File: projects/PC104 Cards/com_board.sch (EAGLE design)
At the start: 7 parts, among them J2 M22-6013005, U2 ESP32-DEVKITC-32D

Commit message: Updated PCB Designs
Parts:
- removed SV1: (no value), con-lsta:FE08-1
- added SV2: (no value), con-lsta:FE12-1
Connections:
- net D18: now also SV2.4; no longer SV1.3
- net D19: now also SV2.3; no longer SV1.2
- net D2: now also SV2.2; no longer SV1.1
- net D21: now also SV2.6; no longer SV1.5
- net D22: now also SV2.7; no longer SV1.6
- net D23: now also SV2.12; no longer SV1.8
- net D4: now also SV2.5; no longer SV1.4
- net GND1: now also SV2.11; no longer SV1.7
- net GND2: now also SV2.10
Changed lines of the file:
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@@
 <part name="H3" library="holes" library_urn="urn:adsk.eagle:library:237" deviceset="MOUNT-PAD-ROUND" device="3.2" package3d_urn="urn:adsk.eagle:package:14282/1"/>
 <part name="H4" library="holes" library_urn="urn:adsk.eagle:library:237" deviceset="MOUNT-PAD-ROUND" device="3.2" package3d_urn="urn:adsk.eagle:package:14282/1"/>
-<part name="SV1" library="con-lsta" library_urn="urn:adsk.eagle:library:161" deviceset="FE08-1" device="" package3d_urn="urn:adsk.eagle:package:8194/1"/>
 <part name="U2" library="ESP32-DEVKITC-32D" deviceset="ESP32-DEVKITC-32D" device=""/>
 <part name="J2" library="M22-6013005" deviceset="M22-6013005" device=""/>
+<part name="SV2" library="con-lsta" library_urn="urn:adsk.eagle:library:161" deviceset="FE12-1" device="" package3d_urn="urn:adsk.eagle:package:8193/1"/>
 </parts>
 <sheets>
@@
 <attribute name="VALUE" x="283.464" y="-102.7938" size="1.778" layer="96"/>
 </instance>
-<instance part="SV1" gate="G$1" x="414.02" y="-76.2" smashed="yes">
-<attribute name="VALUE" x="412.75" y="-88.9" size="1.778" layer="96"/>
-<attribute name="NAME" x="412.75" y="-62.738" size="1.778" layer="95"/>
-</instance>
 <instance part="U2" gate="G$1" x="353.06" y="68.58" smashed="yes">
 <attribute name="NAME" x="337.8028" y="94.6443" size="1.78" layer="95"/>
@@
 <attribute name="NAME" x="502.92" y="13.208" size="1.778" layer="95" rot="R180"/>
 <attribute name="VALUE" x="502.92" y="168.91" size="1.778" layer="96" rot="R180"/>
+</instance>
+<instance part="SV2" gate="G$1" x="368.3" y="-78.74" smashed="yes">
+<attribute name="VALUE" x="367.03" y="-96.52" size="1.778" layer="96"/>
+<attribute name="NAME" x="367.03" y="-60.198" size="1.778" layer="95"/>
 </instance>
 </instances>
@@
 <net name="GND1" class="0">
 <segment>
-<wire x1="421.64" y1="-68.58" x2="431.8" y2="-68.58" width="0.1524" layer="91"/>
-<label x="431.8" y="-68.58" size="1.778" layer="95" xref="yes"/>
-<pinref part="SV1" gate="G$1" pin="7"/>
+<pinref part="SV2" gate="G$1" pin="11"/>
+<wire x1="375.92" y1="-66.04" x2="388.62" y2="-66.04" width="0.1524" layer="91"/>
+<label x="388.62" y="-66.04" size="1.778" layer="95" xref="yes"/>
 </segment>
 </net>
@@
 <label x="513.08" y="46.99" size="1.778" layer="95" xref="yes"/>
 </segment>
+<segment>
+<pinref part="SV2" gate="G$1" pin="10"/>
+<wire x1="375.92" y1="-68.58" x2="381" y2="-68.58" width="0.1524" layer="91"/>
+<label x="381" y="-68.58" size="1.778" layer="95" xref="yes"/>
+</segment>
 </net>
 <net name="GND4" class="0">
@@
 <net name="D23" class="0">
 <segment>
-<wire x1="421.64" y1="-66.04" x2="441.96" y2="-66.04" width="0.1524" layer="91"/>
-<label x="441.96" y="-66.04" size="1.778" layer="95" xref="yes"/>
-<pinref part="SV1" gate="G$1" pin="8"/>
-</segment>
-<segment>
 <pinref part="U2" gate="G$1" pin="IO0"/>
 <wire x1="373.38" y1="58.42" x2="381" y2="58.42" width="0.1524" layer="91"/>
 <label x="381" y="58.42" size="1.27" layer="95" xref="yes"/>
 </segment>
+<segment>
+<pinref part="SV2" gate="G$1" pin="12"/>
+<wire x1="375.92" y1="-63.5" x2="381" y2="-63.5" width="0.1524" layer="91"/>
+<label x="381" y="-63.5" size="1.778" layer="95" xref="yes"/>
+</segment>
 </net>
 <net name="D22" class="0">
-<segment>
-<wire x1="421.64" y1="-71.12" x2="424.18" y2="-71.12" width="0.1524" layer="91"/>
-<label x="424.18" y="-71.12" size="1.778" layer="95" xref="yes"/>
-<pinref part="SV1" gate="G$1" pin="6"/>
-</segment>
 <segment>
 <pinref part="U2" gate="G$1" pin="IO2"/>
@@
 <label x="381" y="55.88" size="1.27" layer="95" xref="yes"/>
 </segment>
+<segment>
+<pinref part="SV2" gate="G$1" pin="7"/>
+<wire x1="375.92" y1="-76.2" x2="388.62" y2="-76.2" width="0.1524" layer="91"/>
+<label x="388.62" y="-76.2" size="1.778" layer="95" xref="yes"/>
+</segment>
 </net>
 <net name="D21" class="0">
-<segment>
-<wire x1="421.64" y1="-73.66" x2="441.96" y2="-73.66" width="0.1524" layer="91"/>
-<label x="441.96" y="-73.66" size="1.778" layer="95" xref="yes"/>
-<pinref part="SV1" gate="G$1" pin="5"/>
-</segment>
 <segment>
 <pinref part="U2" gate="G$1" pin="IO15"/>
@@
 <label x="381" y="53.34" size="1.27" layer="95" xref="yes"/>
 </segment>
+<segment>
+<pinref part="SV2" gate="G$1" pin="6"/>
+<wire x1="375.92" y1="-78.74" x2="381" y2="-78.74" width="0.1524" layer="91"/>
+<label x="381" y="-78.74" size="1.778" layer="95" xref="yes"/>
+</segment>
 </net>
 <net name="D19" class="0">
-<segment>
-<wire x1="421.64" y1="-81.28" x2="441.96" y2="-81.28" width="0.1524" layer="91"/>
-<label x="441.96" y="-81.28" size="1.778" layer="95" xref="yes"/>
-<pinref part="SV1" gate="G$1" pin="2"/>
-</segment>
 <segment>
 <pinref part="U2" gate="G$1" pin="IO14"/>
@@
 <label x="294.64" y="63.5" size="1.27" layer="95" rot="R180" xref="yes"/>
 </segment>
+<segment>
+<pinref part="SV2" gate="G$1" pin="3"/>
+<wire x1="375.92" y1="-86.36" x2="388.62" y2="-86.36" width="0.1524" layer="91"/>
+<label x="388.62" y="-86.36" size="1.778" layer="95" xref="yes"/>
+</segment>
 </net>
 <net name="D18" class="0">
-<segment>
-<wire x1="421.64" y1="-78.74" x2="424.18" y2="-78.74" width="0.1524" layer="91"/>
-<label x="424.18" y="-78.74" size="1.778" layer="95" xref="yes"/>
-<pinref part="SV1" gate="G$1" pin="3"/>
-</segment>
 <segment>
 <pinref part="U2" gate="G$1" pin="IO13"/>
@@
 <label x="312.42" y="55.88" size="1.27" layer="95" rot="R180" xref="yes"/>
 </segment>
+<segment>
+<pinref part="SV2" gate="G$1" pin="4"/>
+<wire x1="375.92" y1="-83.82" x2="381" y2="-83.82" width="0.1524" layer="91"/>
+<label x="381" y="-83.82" size="1.778" layer="95" xref="yes"/>
+</segment>
 </net>
 <net name="D4" class="0">
-<segment>
-<wire x1="421.64" y1="-76.2" x2="434.34" y2="-76.2" width="0.1524" layer="91"/>
-<label x="434.34" y="-76.2" size="1.778" layer="95" xref="yes"/>
-<pinref part="SV1" gate="G$1" pin="4"/>
-</segment>
 <segment>
 <pinref part="U2" gate="G$1" pin="IO27"/>
@@
 <label x="294.64" y="66.04" size="1.27" layer="95" rot="R180" xref="yes"/>
 </segment>
+<segment>
+<pinref part="SV2" gate="G$1" pin="5"/>
+<wire x1="375.92" y1="-81.28" x2="388.62" y2="-81.28" width="0.1524" layer="91"/>
+<label x="388.62" y="-81.28" size="1.778" layer="95" xref="yes"/>
+</segment>
 </net>
 <net name="D2" class="0">
-<segment>
-<wire x1="421.64" y1="-83.82" x2="431.8" y2="-83.82" width="0.1524" layer="91"/>
-<label x="431.8" y="-83.82" size="1.778" layer="95" xref="yes"/>
-<pinref part="SV1" gate="G$1" pin="1"/>
-</segment>
 <segment>
 <pinref part="U2" gate="G$1" pin="IO5"/>
@@
 <label x="375.92" y="68.58" size="1.27" layer="95" xref="yes"/>
 </segment>
-</net>
+<segment>
+<pinref part="SV2" gate="G$1" pin="2"/>
+<wire x1="375.92" y1="-88.9" x2="381" y2="-88.9" width="0.1524" layer="91"/>
+<label x="381" y="-88.9" size="1.778" layer="95" xref="yes"/>
+</segment>
+</net>

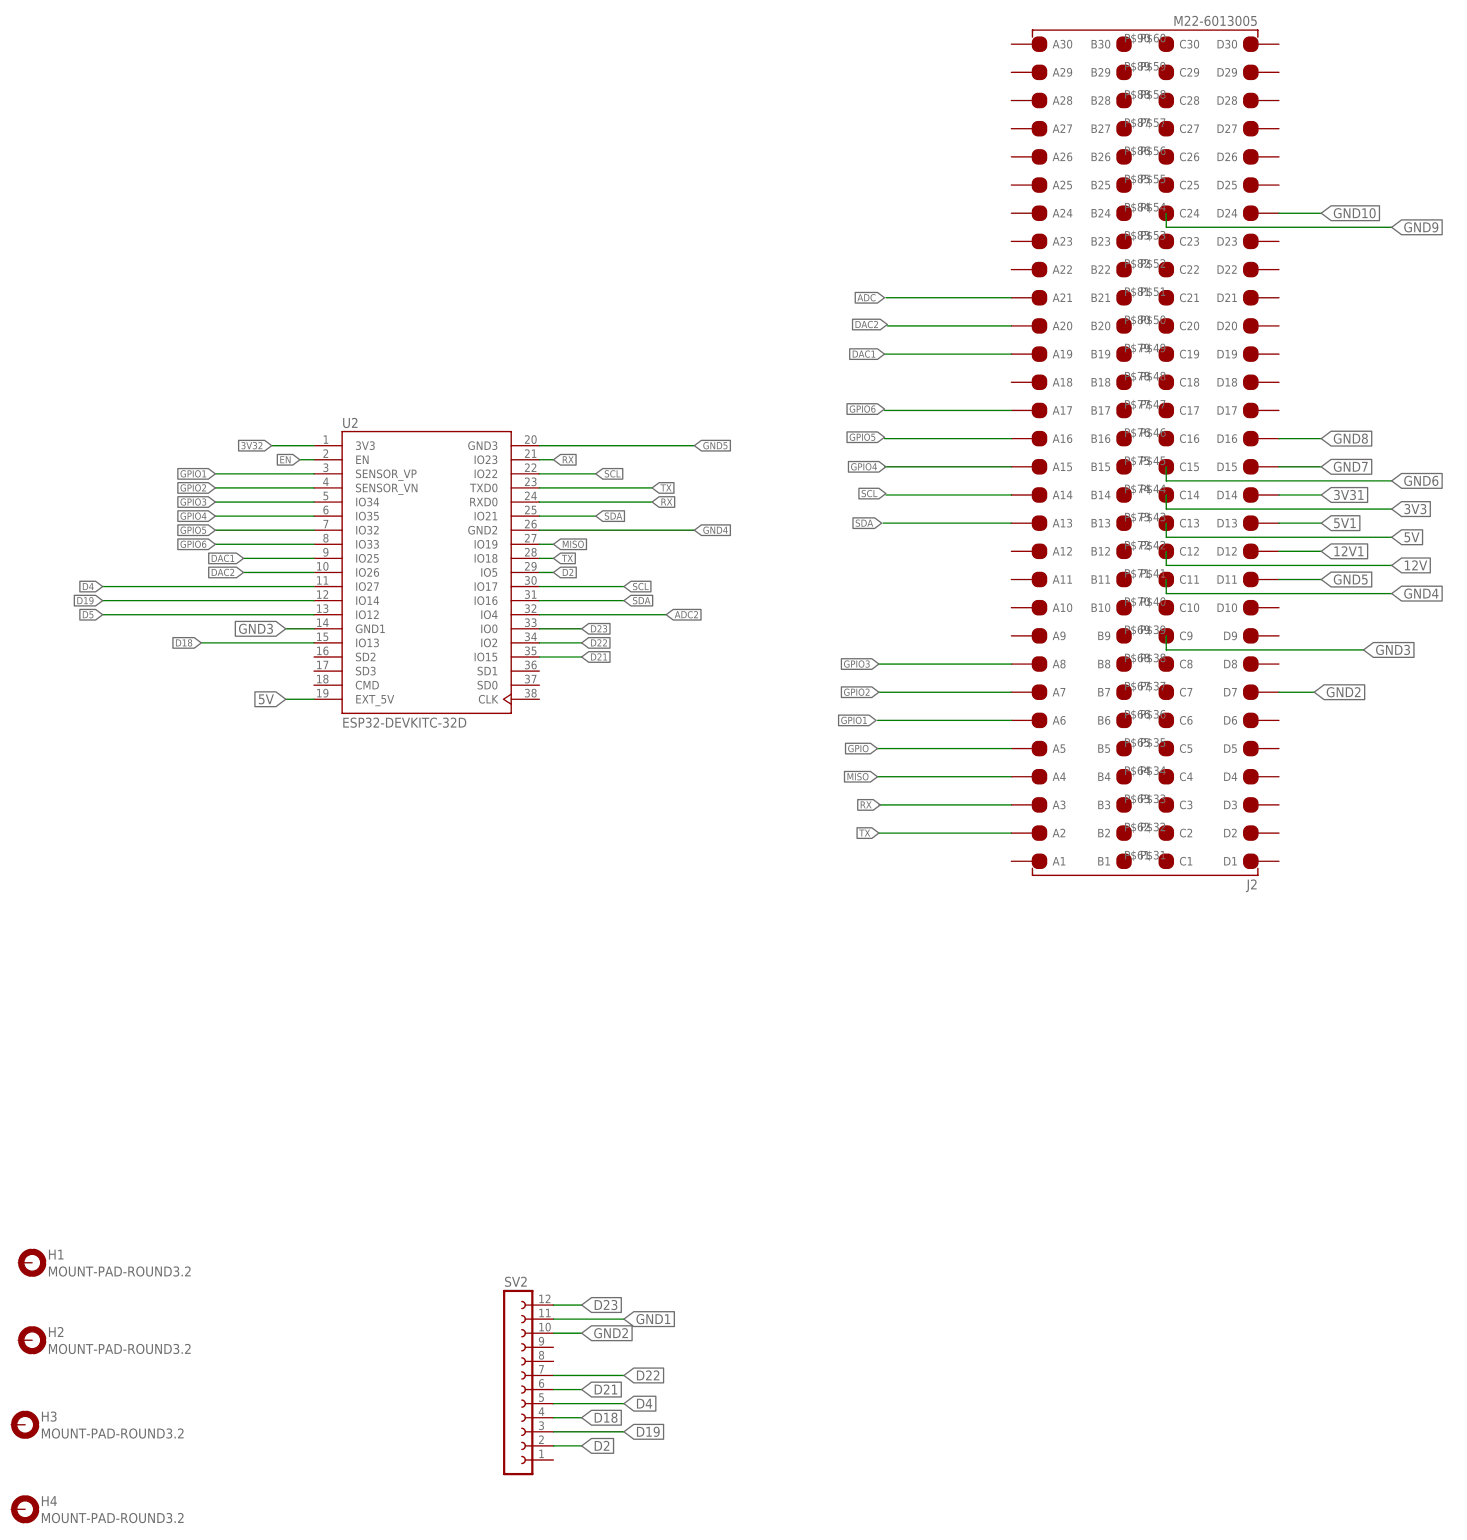
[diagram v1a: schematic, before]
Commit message: Updated PCB desgins to fix wiring mismatches
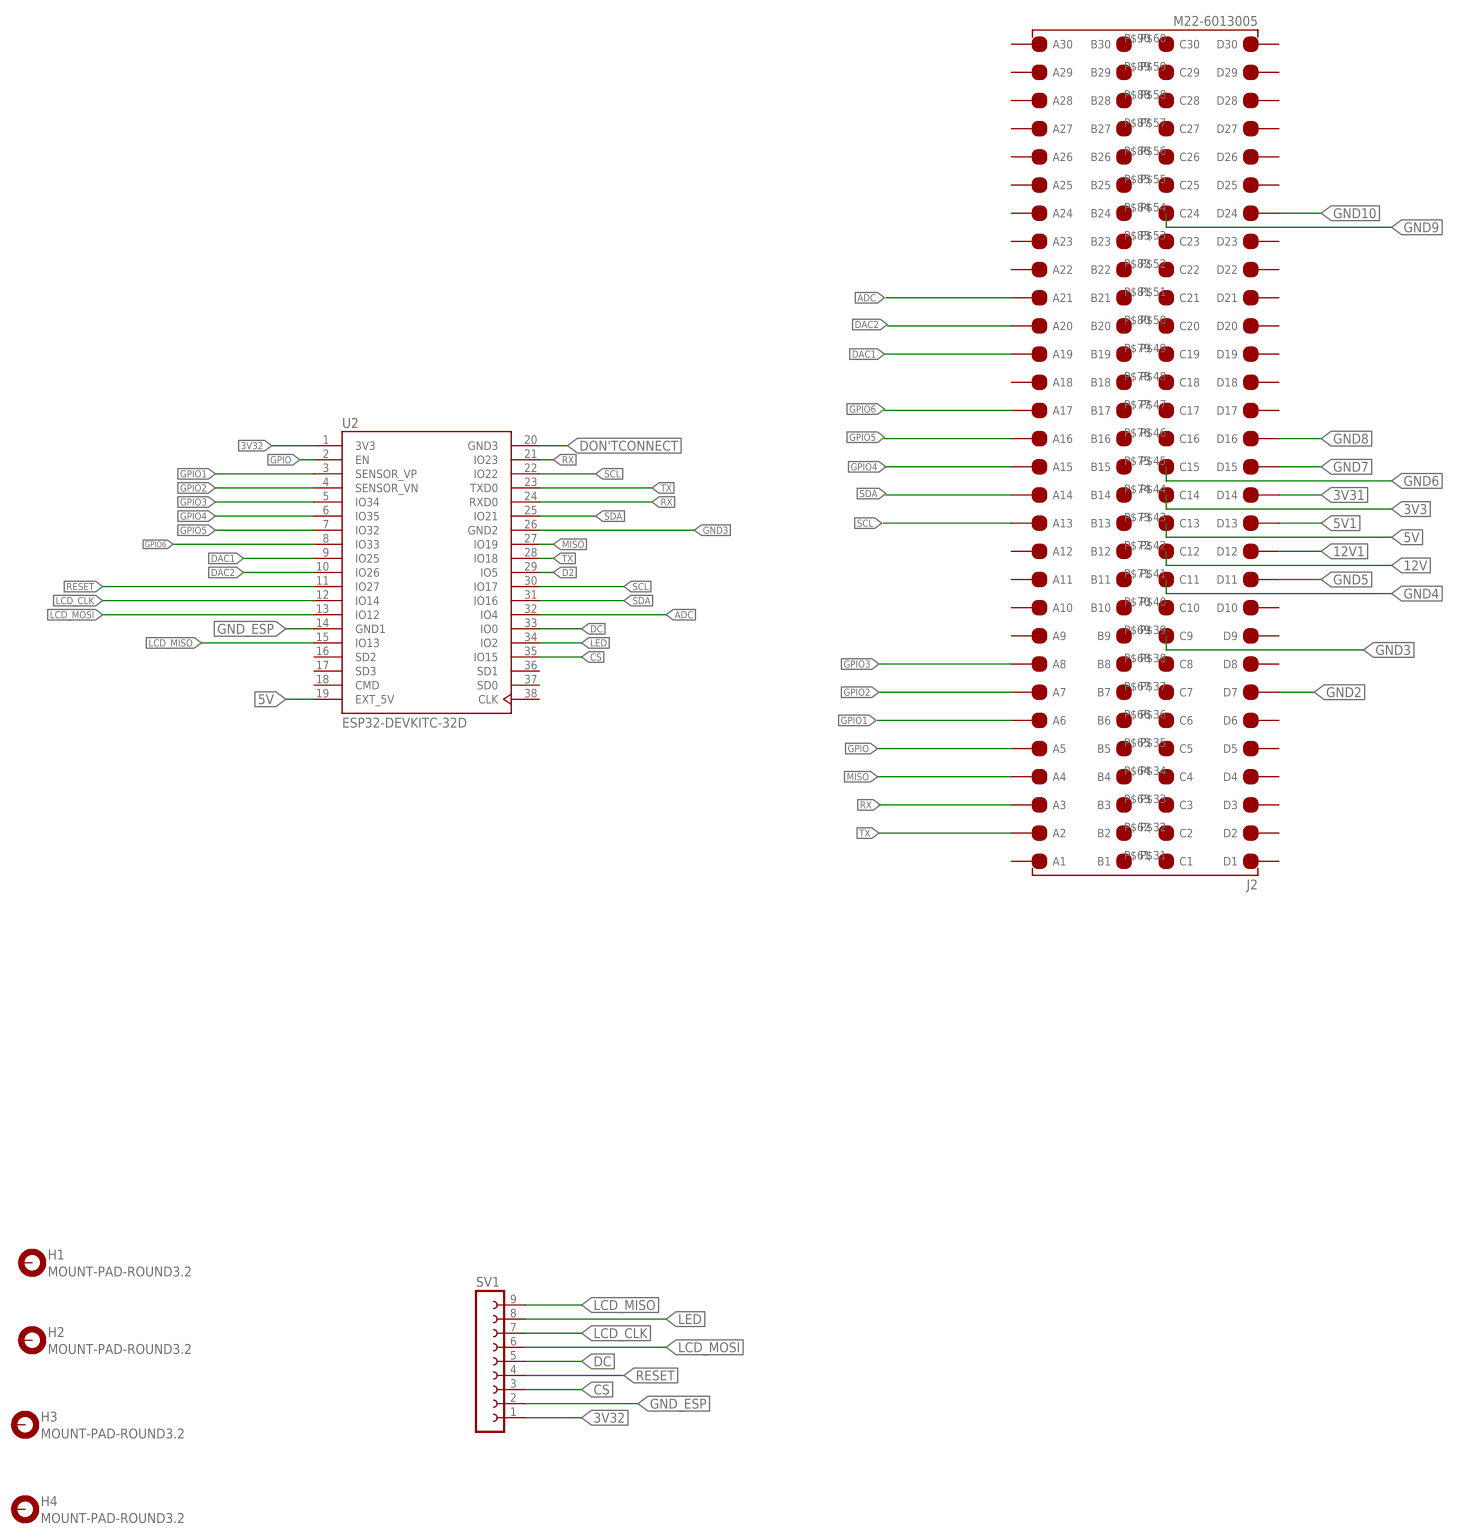
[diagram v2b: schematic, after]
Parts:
- removed SV2: (no value), con-lsta:FE12-1
- added SV1: (no value), con-lsta:FE09-1
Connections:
- removed net ADC2: U2.IO4
- removed net D18: SV2.4, U2.IO13
- removed net D19: SV2.3, U2.IO14
- removed net D21: SV2.6, U2.IO15
- removed net D22: SV2.7, U2.IO2
- removed net D23: SV2.12, U2.IO0
- removed net D4: SV2.5, U2.IO27
- removed net D5: U2.IO12
- removed net EN: U2.EN
- removed net GND1: SV2.11
- new net CS: SV1.3, U2.IO15
- new net DC: SV1.5, U2.IO0
- new net DON'TCONNECT: U2.GND3
- new net GND_ESP: SV1.2, U2.GND1
- new net LCD_CLK: SV1.7, U2.IO14
- new net LCD_MISO: SV1.9, U2.IO13
- new net LCD_MOSI: SV1.6, U2.IO12
- new net LED: SV1.8, U2.IO2
- new net RESET: SV1.4, U2.IO27
- net 3V32: now also SV1.1
- net ADC: now also U2.IO4
- net D2: no longer SV2.2
- net GND2: no longer SV2.10
- net GND3: now also U2.GND2; no longer U2.GND1
- net GND4: no longer U2.GND2
- net GND5: no longer U2.GND3
- net GPIO: now also U2.EN
- net SCL: now also J2.A13; no longer J2.A14
- net SDA: now also J2.A14; no longer J2.A13
